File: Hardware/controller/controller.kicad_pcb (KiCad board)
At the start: 4 copper layers, 128.1 x 184.5 mm, 121 parts, among them J101 Conn_02x10_Odd_Even, J102 Conn_02x10_Odd_Even, J103 Conn_02x10_Odd_Even, J104 Conn_02x08_Odd_Even, J301 Conn_ARM_JTAG_SWD_10, J302 Conn_01x03_Male, M101 Fan_4pin, Q101 MMBT3904, Q301 MMBT3904, SW301 B3F-1005, SW302 B3F-1002, SW303 228ADS2AAWFCMBA, U101 PCA9543A, U102 EMC2101-R, U201 BD9C301FJ, U302 ATSAME51J20A-A, U303 AT25SF321B-SSHB, U401 KSZ8041TL, X401 50MHz, Y301 32.768kHz, Y302 12MHz

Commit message: Reworked /I2C_IRQ line
- Moved the /I2C_IRQ signal to PA10 so that it no longer conflicts with
  the external interrupt (EIC) input line for the encoder at PB07.

- Remove the superfluous UART header, as we're not actually going to use
  the UART for anything. This will all take place over USB CDC instead,
  and use SWD for early boot output.
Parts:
- removed J302: Conn_01x03_Male, Connector_PinHeader_2.54mm:PinHeader_1x03_P2.54mm_Vertical
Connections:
- U302 pad 16: /~{I2C_IRQ} -> unconnected-(U302-Pad16)
- U302 pad 19: /CPU/TTY_TXD -> /~{I2C_IRQ}
- U302 pad 20: /CPU/TTY_RXD -> unconnected-(U302-Pad20)
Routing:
- net /CPU/TTY_TXD: track 14.4 -> 0.00 mm
- net /CPU/TTY_RXD: track 12.5 -> 0.00 mm
- net /~{I2C_IRQ}: track 20.6 -> 19.1 mm
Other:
- board text added: "Rev 2"
- board text removed: "GND"
- board text removed: "RXD"
- board text removed: "Rev 1"
- board text removed: "TXD"
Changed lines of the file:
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@@
   )
   (paper "A4" portrait)
+  (title_block
+    (title "Programmable Load Controller")
+    (date "2022-03-20")
+    (rev "2")
+    (company "Tristan Seifert")
+  )
   (layers
     (0 "F.Cu" signal)
@@
   (net 25 "/FRONT_ENC_B")
   (net 26 "/~{FRONT_IRQ}")
-  (net 27 "/CPU/TTY_TXD")
-  (net 28 "/CPU/TTY_RXD")
+  (net 27 "unconnected-(U302-Pad16)")
+  (net 28 "unconnected-(U302-Pad20)")
   (net 29 "/~{FRONT_RESET}")
   (net 30 "/DISP_D{slash}~{C}")
@@
       (net 73 "/~{I2C_RESET}") (pinfunction "PA06") (pintype "bidirectional"))
     (pad "16" smd roundrect (at -5.6625 3.75) (size 1.475 0.3) (layers "F.Cu" "F.Paste" "F.Mask") (roundrect_rratio 0.25)
-      (net 74 "/~{I2C_IRQ}") (pinfunction "PA07") (pintype "bidirectional"))
+      (net 27 "unconnected-(U302-Pad16)") (pinfunction "PA07") (pintype "bidirectional+no_connect"))
     (pad "17" smd roundrect (at -3.75 5.6625) (size 0.3 1.475) (layers "F.Cu" "F.Paste" "F.Mask") (roundrect_rratio 0.25)
       (net 76 "/I2C_SDA") (pinfunction "PA08") (pintype "bidirectional"))
@@
       (net 75 "/I2C_SCL") (pinfunction "PA09") (pintype "bidirectional"))
     (pad "19" smd roundrect (at -2.75 5.6625) (size 0.3 1.475) (layers "F.Cu" "F.Paste" "F.Mask") (roundrect_rratio 0.25)
-      (net 27 "/CPU/TTY_TXD") (pinfunction "PA10") (pintype "bidirectional"))
+      (net 74 "/~{I2C_IRQ}") (pinfunction "PA10") (pintype "bidirectional"))
     (pad "20" smd roundrect (at -2.25 5.6625) (size 0.3 1.475) (layers "F.Cu" "F.Paste" "F.Mask") (roundrect_rratio 0.25)
-      (net 28 "/CPU/TTY_RXD") (pinfunction "PA11") (pintype "bidirectional"))
+      (net 28 "unconnected-(U302-Pad20)") (pinfunction "PA11") (pintype "bidirectional+no_connect"))
     (pad "21" smd roundrect (at -1.75 5.6625) (size 0.3 1.475) (layers "F.Cu" "F.Paste" "F.Mask") (roundrect_rratio 0.25)
       (net 59 "+3V3") (pinfunction "VDDIOB") (pintype "power_in"))
@@
     )
   )
-  (footprint "Connector_PinHeader_2.54mm:PinHeader_1x03_P2.54mm_Vertical" (layer "F.Cu")
-    (at 70.8 61.4 -90)
-    (descr "Through hole straight pin header, 1x03, 2.54mm pitch, single row")
-    (tags "Through hole pin header THT 1x03 2.54mm single row")
-    (property "Sheetfile" "cpu.kicad_sch")
-    (property "Sheetname" "CPU")
-    (attr through_hole)
-    (fp_text reference "J302" (at 0 -2.33 90) (layer "F.SilkS")
-      (effects (font (size 1 1) (thickness 0.15)))
-    )
-    (fp_text value "Conn_01x03_Male" (at 0 7.41 90) (layer "F.Fab") hide
-      (effects (font (size 1 1) (thickness 0.15)))
-    )
-    (fp_text user "${REFERENCE}" (at 0 2.54) (layer "F.Fab")
-      (effects (font (size 1 1) (thickness 0.15)))
-    )
-    (fp_line (start -1.33 1.27) (end 1.33 1.27) (layer "F.SilkS") (width 0.12))
-    (fp_line (start -1.33 -1.33) (end 0 -1.33) (layer "F.SilkS") (width 0.12))
-    (fp_line (start -1.33 1.27) (end -1.33 6.41) (layer "F.SilkS") (width 0.12))
-    (fp_line (start -1.33 6.41) (end 1.33 6.41) (layer "F.SilkS") (width 0.12))
-    (fp_line (start 1.33 1.27) (end 1.33 6.41) (layer "F.SilkS") (width 0.12))
-    (fp_line (start -1.33 0) (end -1.33 -1.33) (layer "F.SilkS") (width 0.12))
-    (fp_line (start 1.8 -1.8) (end -1.8 -1.8) (layer "F.CrtYd") (width 0.05))
-    (fp_line (start 1.8 6.85) (end 1.8 -1.8) (layer "F.CrtYd") (width 0.05))
-    (fp_line (start -1.8 6.85) (end 1.8 6.85) (layer "F.CrtYd") (width 0.05))
-    (fp_line (start -1.8 -1.8) (end -1.8 6.85) (layer "F.CrtYd") (width 0.05))
-    (fp_line (start 1.27 6.35) (end -1.27 6.35) (layer "F.Fab") (width 0.1))
-    (fp_line (start 1.27 -1.27) (end 1.27 6.35) (layer "F.Fab") (width 0.1))
-    (fp_line (start -1.27 6.35) (end -1.27 -0.635) (layer "F.Fab") (width 0.1))
-    (fp_line (start -1.27 -0.635) (end -0.635 -1.27) (layer "F.Fab") (width 0.1))
-    (fp_line (start -0.635 -1.27) (end 1.27 -1.27) (layer "F.Fab") (width 0.1))
-    (pad "1" thru_hole rect (at 0 0 270) (size 1.7 1.7) (drill 1) (layers *.Cu *.Mask)
-      (net 28 "/CPU/TTY_RXD") (pinfunction "Pin_1") (pintype "passive"))
-    (pad "2" thru_hole oval (at 0 2.54 270) (size 1.7 1.7) (drill 1) (layers *.Cu *.Mask)
-      (net 27 "/CPU/TTY_TXD") (pinfunction "Pin_2") (pintype "passive"))
-    (pad "3" thru_hole oval (at 0 5.08 270) (size 1.7 1.7) (drill 1) (layers *.Cu *.Mask)
-      (net 1 "GND") (pinfunction "Pin_3") (pintype "passive"))
-    (model "${KICAD6_3DMODEL_DIR}/Connector_PinHeader_2.54mm.3dshapes/PinHeader_1x03_P2.54mm_Vertical.wrl"
-      (offset (xyz 0 0 0))
-      (scale (xyz 1 1 1))
-      (rotate (xyz 0 0 0))
-    )
-  )
   (footprint "Capacitor_SMD:C_0805_2012Metric_Pad1.18x1.45mm_HandSolder" (layer "F.Cu")
     (at 83.7 34.8)
@@
   (gr_line (start 20 20) (end 148.13 20) (layer "Edge.Cuts") (width 0.1))
   (gr_line (start 20 20) (end 20 204.5) (layer "Edge.Cuts") (width 0.1))
-  (gr_text "GND" (at 65.7 63.2 270) (layer "B.SilkS")
-    (effects (font (size 1.27 1.27) (thickness 0.15)) (justify right mirror))
-  )
-  (gr_text "TXD" (at 68.3 63.2 270) (layer "B.SilkS")
-    (effects (font (size 1.27 1.27) (thickness 0.15)) (justify right mirror))
-  )
-  (gr_text "RXD" (at 70.8 63.2 270) (layer "B.SilkS")
-    (effects (font (size 1.27 1.27) (thickness 0.15)) (justify right mirror))
-  )
   (gr_text "Display" (at 51.1 142.7) (layer "F.SilkS")
     (effects (font (size 1.5 1.5) (thickness 0.25)))
@@
     (effects (font (size 1.74 1.74) (thickness 0.25)) (justify right))
   )
-  (gr_text "Rev 1" (at 138.75 145 90) (layer "F.SilkS")
+  (gr_text "Rev 2" (at 138.75 145 90) (layer "F.SilkS")
     (effects (font (size 2 2) (thickness 0.2)))
   )
@@
   (segment (start 41.8 166.1275) (end 41.8 165.9) (width 0.2032) (layer "B.Cu") (net 26))
   (segment (start 35.2275 165.6) (end 35.2 165.6275) (width 0.2032) (layer "B.Cu") (net 26))
-  (segment (start 75.196014 56.67028) (end 70.17972 56.67028) (width 0.2032) (layer "F.Cu") (net 27))
-  (segment (start 70.17972 56.67028) (end 68.26 58.59) (width 0.2032) (layer "F.Cu") (net 27))
-  (segment (start 77.25 54.616294) (end 75.196014 56.67028) (width 0.2032) (layer "F.Cu") (net 27))
-  (segment (start 77.25 53.6625) (end 77.25 54.616294) (width 0.2032) (layer "F.Cu") (net 27))
-  (segment (start 68.26 58.59) (end 68.26 61.4) (width 0.2032) (layer "F.Cu") (net 27))
-  (segment (start 75.332588 57) (end 72.05 57) (width 0.2032) (layer "F.Cu") (net 28))
-  (segment (start 77.75 54.582588) (end 75.332588 57) (width 0.2032) (layer "F.Cu") (net 28))
-  (segment (start 70.8 58.25) (end 70.8 61.4) (width 0.2032) (layer "F.Cu") (net 28))
-  (segment (start 72.05 57) (end 70.8 58.25) (width 0.2032) (layer "F.Cu") (net 28))
-  (segment (start 77.75 53.6625) (end 77.75 54.582588) (width 0.2032) (layer "F.Cu") (net 28))
   (segment (start 42.55 146.4) (end 42.22 146.73) (width 0.2032) (layer "F.Cu") (net 29))
   (segment (start 72.448882 50.75) (end 74.3375 50.75) (width 0.2032) (layer "F.Cu") (net 29))
@@
   (segment (start 54.1375 55.85) (end 55.55 55.85) (width 0.2032) (layer "F.Cu") (net 73))
   (segment (start 55.8 54.4) (end 57.281121 52.918879) (width 0.2032) (layer "F.Cu") (net 73))
-  (segment (start 58.6 56.35) (end 58.75 56.5) (width 0.2032) (layer "F.Cu") (net 74))
-  (segment (start 74.3375 51.75) (end 72.38147 51.75) (width 0.2032) (layer "F.Cu") (net 74))
-  (segment (start 70.882872 53.248598) (end 58.951402 53.248598) (width 0.2032) (layer "F.Cu") (net 74))
-  (segment (start 58.951402 53.248598) (end 58.6 53.6) (width 0.2032) (layer "F.Cu") (net 74))
-  (segment (start 58.6 53.6) (end 58.6 56.35) (width 0.2032) (layer "F.Cu") (net 74))
-  (segment (start 72.38147 51.75) (end 70.882872 53.248598) (width 0.2032) (layer "F.Cu") (net 74))
-  (segment (start 58.75 56.5) (end 59.8625 56.5) (width 0.2032) (layer "F.Cu") (net 74))
+  (segment (start 59.8625 56.5) (end 75.366294 56.5) (width 0.2032) (layer "F.Cu") (net 74))
+  (segment (start 75.366294 56.5) (end 75.683147 56.183147) (width 0.2032) (layer "F.Cu") (net 74))
+  (segment (start 77.25 53.6625) (end 77.25 54.616294) (width 0.2032) (layer "F.Cu") (net 74))
+  (segment (start 77.25 54.616294) (end 75.683147 56.183147) (width 0.2032) (layer "F.Cu") (net 74))
   (segment (start 75.55 55.85) (end 59.8625 55.85) (width 0.2032) (layer "F.Cu") (net 75))
   (segment (start 76.75 54.65) (end 75.55 55.85) (width 0.2032) (layer "F.Cu") (net 75))

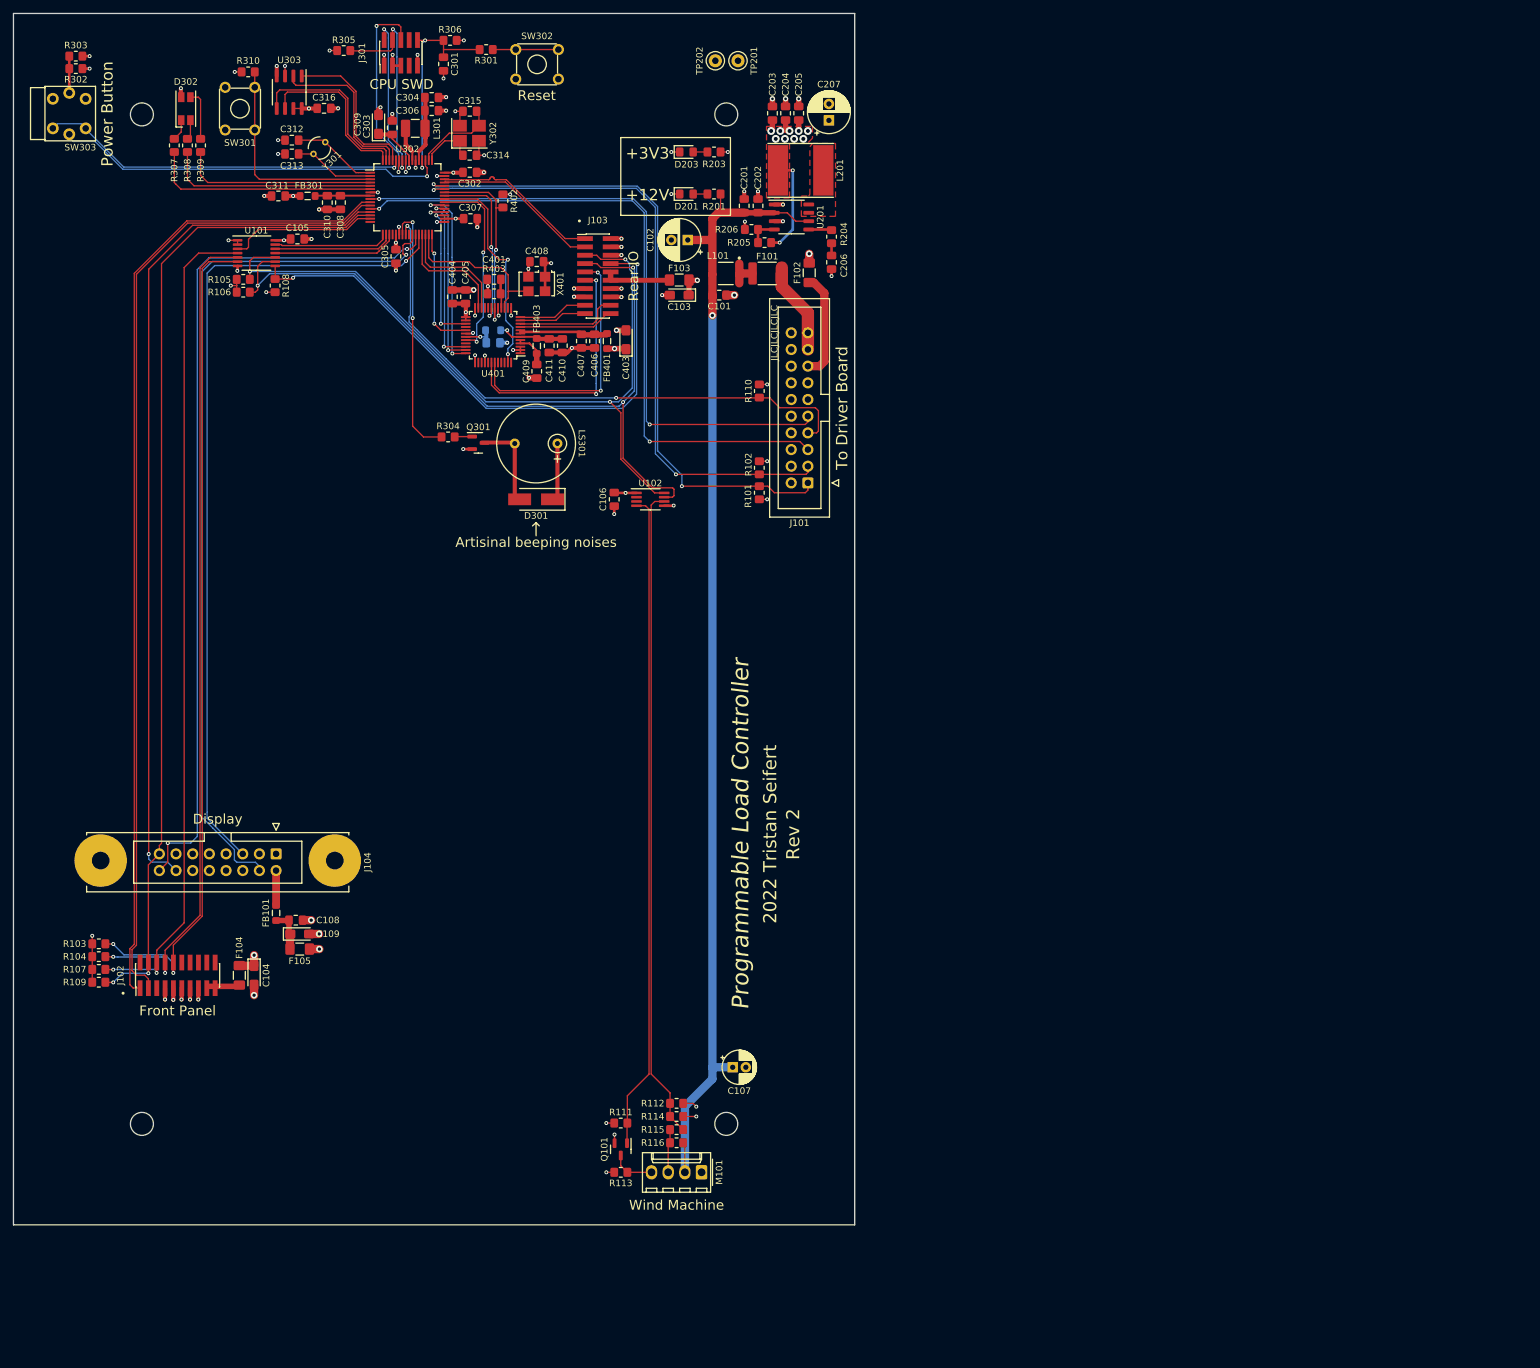
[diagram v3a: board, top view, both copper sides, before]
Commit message: Rev2 fixes for controller board
- Split power button into two separate IO lines

- Fixed missing pull-ups on IO I2C bus, and routed interrupt line
  correctly

- Cutouts for bosses in case on board
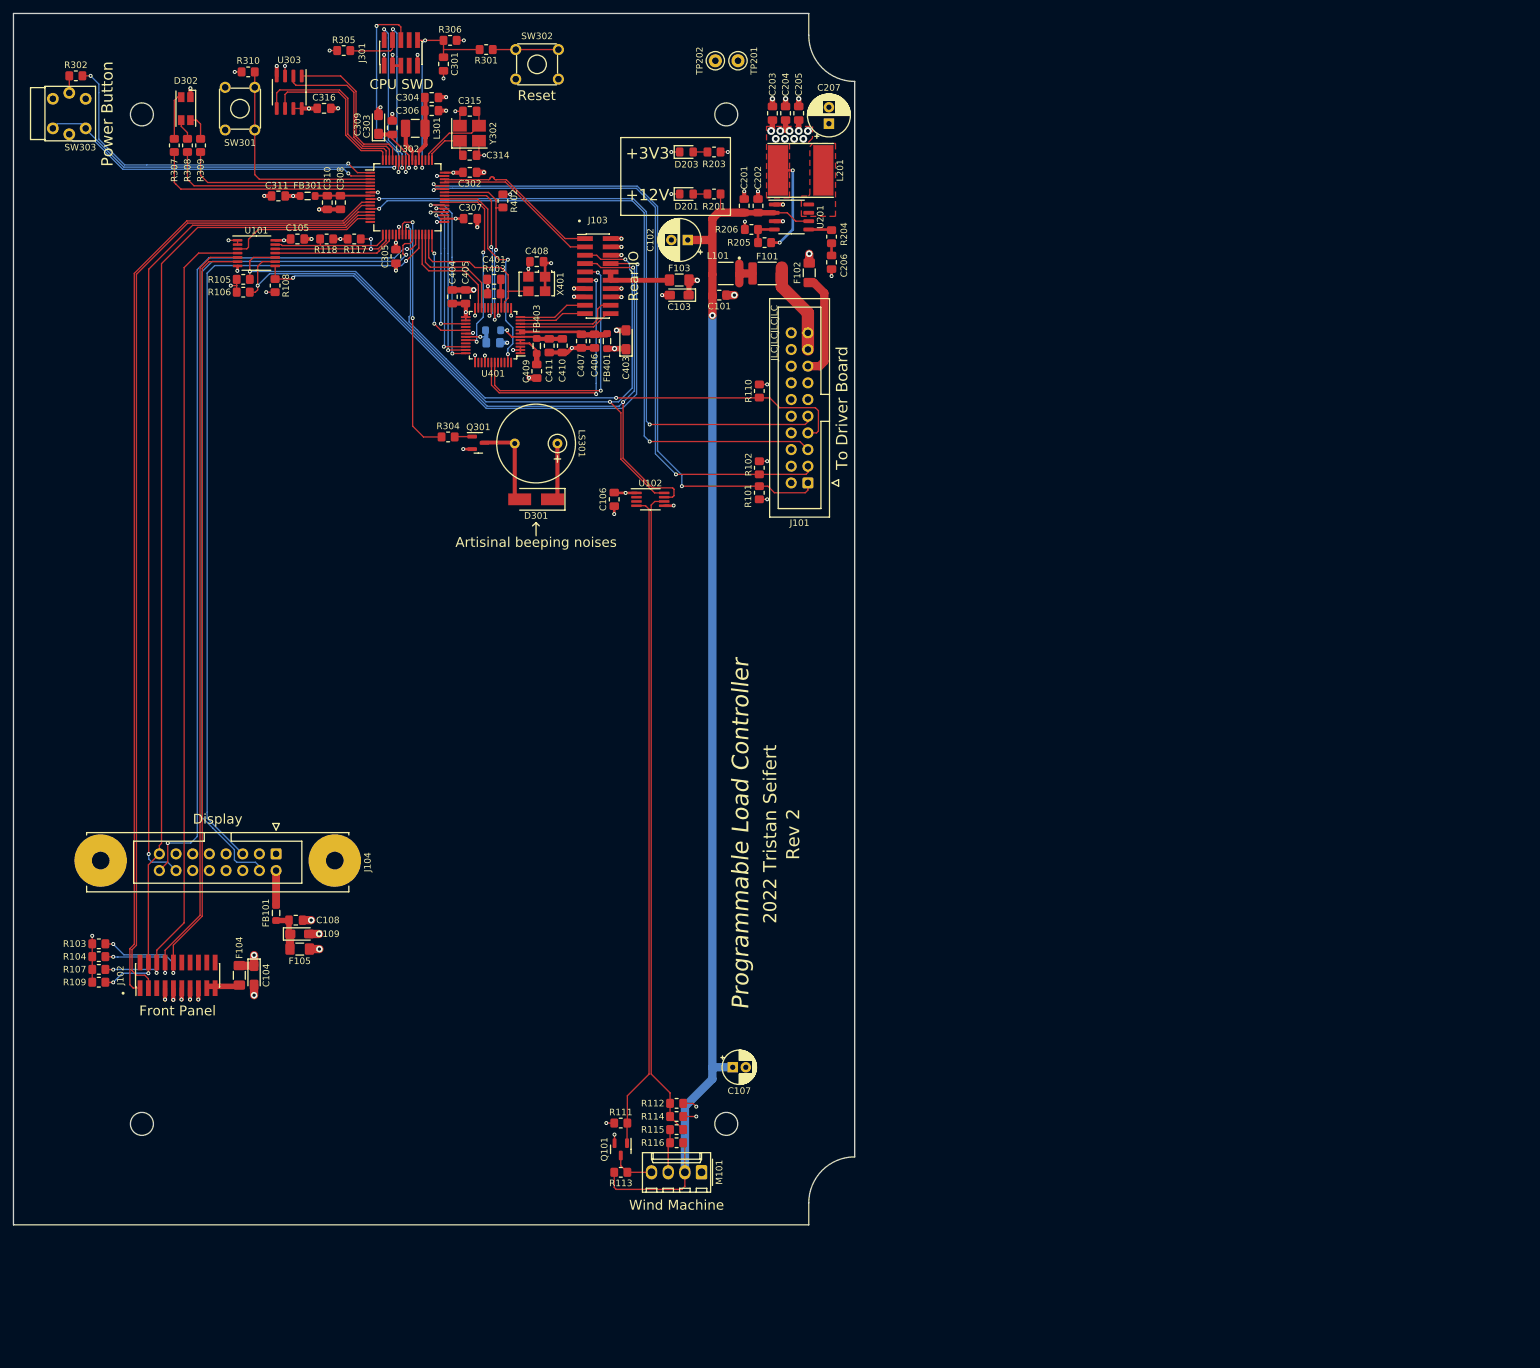
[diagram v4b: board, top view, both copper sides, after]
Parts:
- removed C312, C313: 4.7pF, Capacitor_SMD:C_0805_2012Metric_Pad1.18x1.45mm_HandSolder
- removed R303: 330R, Resistor_SMD:R_0805_2012Metric_Pad1.20x1.40mm_HandSolder
- removed Y301: 32.768kHz, Crystal:Crystal_AT310_D3.0mm_L10.0mm_Vertical
- added R117: 2k2, Resistor_SMD:R_0805_2012Metric_Pad1.20x1.40mm_HandSolder, F.Cu at (71.9, 54.4)
- added R118: 2k2, Resistor_SMD:R_0805_2012Metric_Pad1.20x1.40mm_HandSolder, F.Cu at (67.7, 54.4)
- moved R302 1.10 mm to (29.5, 29.5), turned to 0 degrees
- moved C207 0.50 mm to (144.2, 36.8)
- turned D302 to -90 degrees
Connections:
- D302 pad 1: Net-(D302-Pad1) -> +3V3
- D302 pad 4: +3V3 -> Net-(D302-Pad4)
- R113 pad 2: +3V3 -> +12V
- R302 pad 1: +3V3 -> Net-(R302-Pad1)
- R302 pad 2: Net-(R302-Pad2) -> /CPU/PWRLED1
- R307 pad 1: Net-(D302-Pad1) -> Net-(D302-Pad2)
- R308 pad 1: Net-(D302-Pad2) -> Net-(D302-Pad3)
- R309 pad 1: Net-(D302-Pad3) -> Net-(D302-Pad4)
- SW303 pad L1: /CPU/PWRLED -> /CPU/PWRLED0
- SW303 pad L2: Net-(R302-Pad2) -> Net-(R302-Pad1)
- U302 pad 1: /CPU/X32IN -> /CPU/PWRLED1
- U302 pad 16: unconnected-(U302-Pad16) -> /CPU/FAN_PWM
- U302 pad 2: /CPU/X32OUT -> /CPU/PWRLED0
- U302 pad 51: /CPU/PWRLED -> unconnected-(U302-Pad51)
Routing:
- net /CPU/PWRLED: track 60.0 -> 0.00 mm, vias 1 -> 0
- net /CPU/PWRLED1: track 0.00 -> 55.0 mm, vias 0 -> 2
- net /CPU/PWRLED0: track 0.00 -> 48.8 mm, vias 0 -> 1
- net +12V: track 176.6 -> 192.2 mm
- net /CPU/X32IN: track 13.0 -> 0.00 mm
- net /CPU/X32OUT: track 12.2 -> 0.00 mm
- net Net-(R302-Pad2): track 5.60 -> 0.00 mm
- net Net-(D302-Pad3): track 7.69 -> 3.24 mm
- net Net-(D302-Pad2): track 3.04 -> 7.11 mm
- net Net-(D302-Pad4): track 0.00 -> 4.05 mm
- net Net-(D302-Pad1): track 3.28 -> 0.00 mm
- net GND: track 115.7 -> 112.5 mm, vias 73 -> 70
- net /I2C_SCL: track 18.4 -> 21.5 mm, vias 0 -> 2
- net Net-(R302-Pad1): track 0.00 -> 2.60 mm
- net /I2C_SDA: track 17.6 -> 18.6 mm
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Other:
- outline, holes or cut-outs redrawn
